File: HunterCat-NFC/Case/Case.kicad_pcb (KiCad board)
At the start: 2 copper layers, 88 x 33.5 mm, 4 parts

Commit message: Case
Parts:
- added REF**: MountingHole_2.2mm_M2, MountingHole:MountingHole_2.2mm_M2, F.Cu at (84.4, 119.8)
- added REF**: MountingHole_2.2mm_M2, MountingHole:MountingHole_2.2mm_M2, F.Cu at (189.7, 147.5)
- added REF**: MountingHole_2.2mm_M2, MountingHole:MountingHole_2.2mm_M2, F.Cu at (149.8, 35.4)
- added REF**: MountingHole_2.2mm_M2, MountingHole:MountingHole_2.2mm_M2, F.Cu at (138.4, 35.3)
- added REF**: MountingHole_2.2mm_M2, MountingHole:MountingHole_2.2mm_M2, F.Cu at (138.4, 55.6)
- added REF**: MountingHole_2.2mm_M2, MountingHole:MountingHole_2.2mm_M2, F.Cu at (149.8, 55.6)
- added REF**: MountingHole_2.2mm_M2, MountingHole:MountingHole_2.2mm_M2, F.Cu at (107.9, 31.0)
- added REF**: MountingHole_2.2mm_M2, MountingHole:MountingHole_2.2mm_M2, F.Cu at (188.5, 31.0)
- added REF**: MountingHole_2.2mm_M2, MountingHole:MountingHole_2.2mm_M2, F.Cu at (188.5, 58.7)
- added REF**: MountingHole_2.2mm_M2, MountingHole:MountingHole_2.2mm_M2, F.Cu at (83.2, 58.7)
- added REF**: MountingHole_2.2mm_M2, MountingHole:MountingHole_2.2mm_M2, F.Cu at (107.9, 58.7)
- added REF**: MountingHole_2.2mm_M2, MountingHole:MountingHole_2.2mm_M2, F.Cu at (84.4, 147.5)
- added REF**: MountingHole_2.2mm_M2, MountingHole:MountingHole_2.2mm_M2, F.Cu at (83.2, 31.0)
- added REF**: MountingHole_2.2mm_M2, MountingHole:MountingHole_2.2mm_M2, F.Cu at (83.0, 106.1)
- added REF**: MountingHole_2.2mm_M2, MountingHole:MountingHole_2.2mm_M2, F.Cu at (83.0, 78.4)
- added REF**: MountingHole_2.2mm_M2, MountingHole:MountingHole_2.2mm_M2, F.Cu at (109.1, 147.5)
- added REF**: MountingHole_2.2mm_M2, MountingHole:MountingHole_2.2mm_M2, F.Cu at (109.1, 119.8)
- added REF**: MountingHole_2.2mm_M2, MountingHole:MountingHole_2.2mm_M2, F.Cu at (139.6, 144.4)
- added REF**: MountingHole_2.2mm_M2, MountingHole:MountingHole_2.2mm_M2, F.Cu at (189.7, 119.8)
- added REF**: MountingHole_2.2mm_M2, MountingHole:MountingHole_2.2mm_M2, F.Cu at (151.1, 144.4)
- added REF**: MountingHole_2.2mm_M2, MountingHole:MountingHole_2.2mm_M2, F.Cu at (151.1, 124.2)
- added REF**: MountingHole_2.2mm_M2, MountingHole:MountingHole_2.2mm_M2, F.Cu at (139.6, 124.1)
- moved REF** 36.9 mm to (107.7, 78.4)
- moved REF** 36.9 mm to (107.7, 106.1)
- moved REF** 36.9 mm to (188.2, 106.1)
- moved REF** 36.9 mm to (188.2, 78.4)
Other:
- board size 88 x 33.5 mm -> 113.4 x 122.3 mm

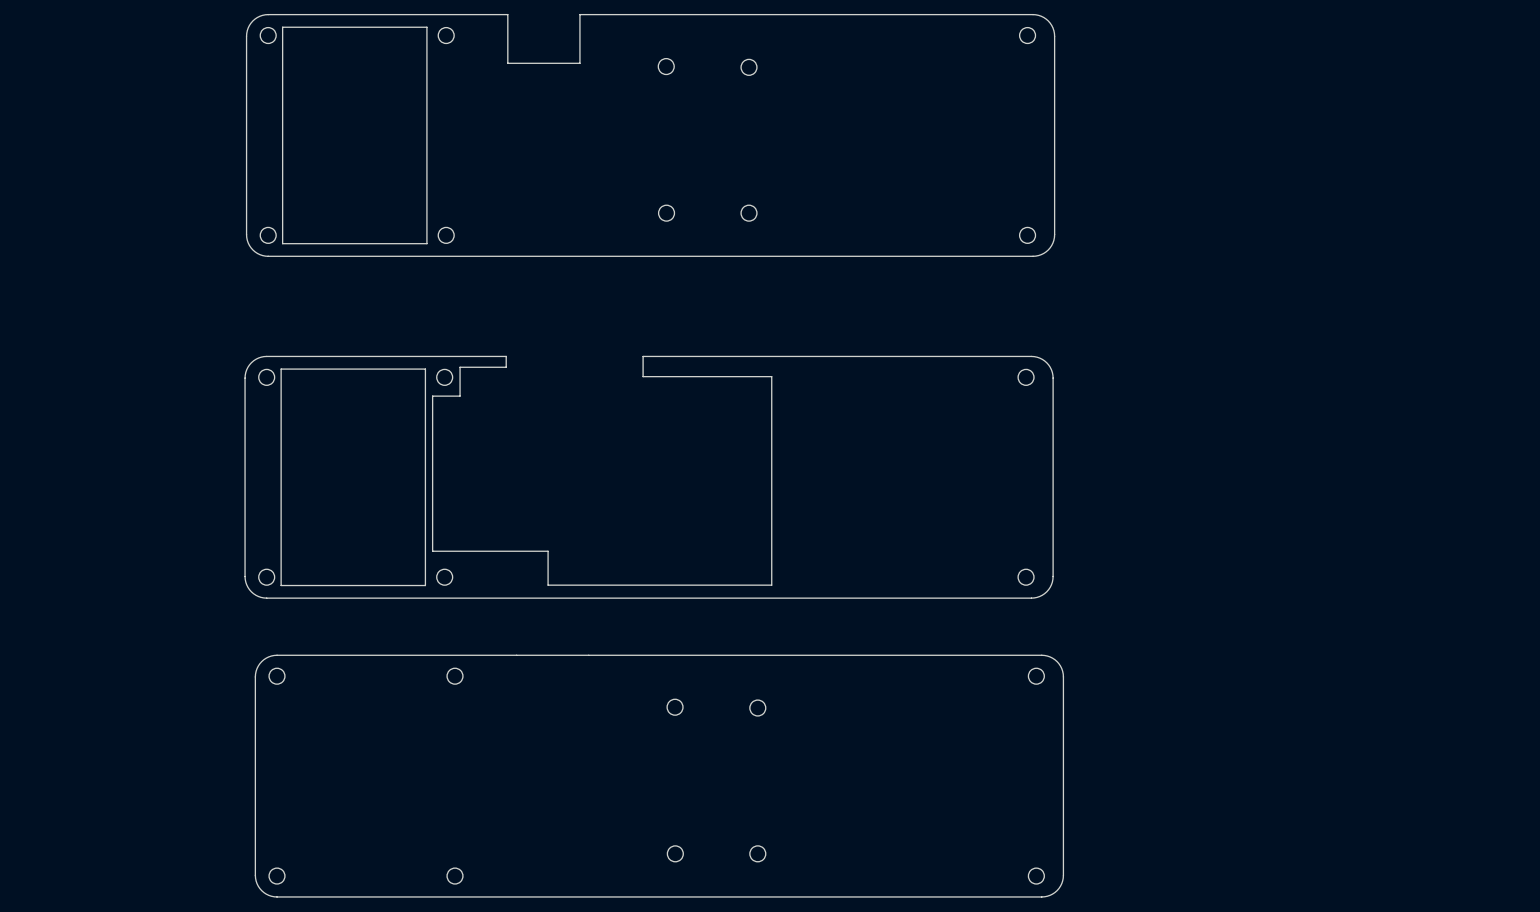
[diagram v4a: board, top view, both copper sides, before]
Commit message: Moved footprints
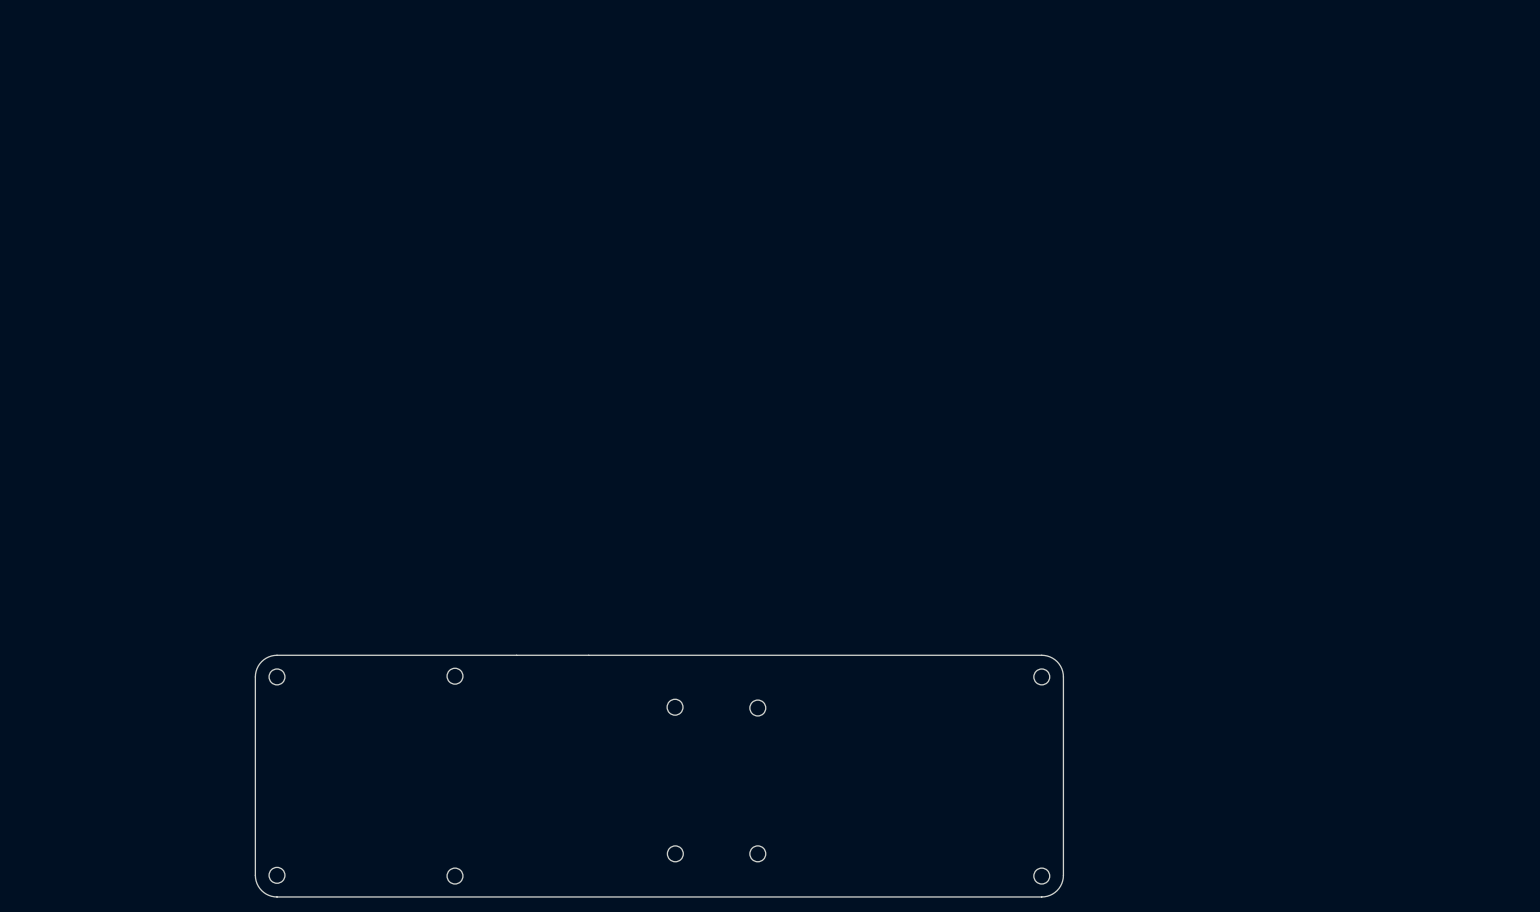
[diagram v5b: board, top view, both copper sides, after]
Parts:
- removed the REF** at (149.8, 35.4)
- removed the REF** at (138.4, 35.3)
- removed the REF** at (138.4, 55.6)
- removed the REF** at (149.8, 55.6)
- removed the REF** at (107.9, 31.0)
- removed the REF** at (188.5, 31.0)
- removed the REF** at (188.5, 58.7)
- removed the REF** at (83.2, 58.7)
- removed the REF** at (107.9, 58.7)
- removed the REF** at (83.2, 31.0)
- removed the REF** at (83.0, 106.1)
- removed the REF** at (83.0, 78.4)
- removed the REF** at (107.7, 106.1)
- removed the REF** at (188.2, 106.1)
- removed the REF** at (188.2, 78.4)
- removed the REF** at (107.7, 78.4)
- moved REF** 0.76 mm to (190.4, 119.9)
- moved REF** 0.75 mm to (190.4, 147.5)
- moved REF** 0.10 mm to (84.4, 147.4)
- moved REF** 0.10 mm to (84.4, 119.9)
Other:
- board size 113.4 x 122.3 mm -> 112 x 33.5 mm

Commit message: Case holes placement
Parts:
- removed the REF** at (109.1, 147.5)
- removed the REF** at (109.1, 119.8)
- moved REF** 31.3 mm to (170.9, 124.2)
- moved REF** 31.3 mm to (182.4, 144.4)
- moved REF** 31.3 mm to (182.4, 124.2)
- moved REF** 31.3 mm to (170.9, 144.4)
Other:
- outline, holes or cut-outs redrawn
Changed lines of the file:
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@@
   (general
     (thickness 1.6)
-    (drawings 10)
+    (drawings 18)
     (tracks 0)
     (zones 0)
-    (modules 10)
+    (modules 8)
     (nets 1)
   )
@@
   )
   (module MountingHole:MountingHole_2.2mm_M2 (layer F.Cu)
-    (at 109.1 147.52)
-    (descr "Mounting Hole 2.2mm, no annular, M2")
-    (tags "mounting hole 2.2mm no annular m2")
-    (attr virtual)
-    (fp_text reference REF** (at 0 -3.2) (layer F.Fab)
-      (effects (font (size 1 1) (thickness 0.15)))
-    )
-    (fp_text value MountingHole_2.2mm_M2 (at 0 3.2) (layer F.Fab)
-      (effects (font (size 1 1) (thickness 0.15)))
-    )
-    (fp_circle (center 0 0) (end 2.2 0) (layer Cmts.User) (width 0.15))
-    (fp_circle (center 0 0) (end 2.45 0) (layer F.CrtYd) (width 0.05))
-    (fp_text user %R (at 0.3 0) (layer F.Fab)
-      (effects (font (size 1 1) (thickness 0.15)))
-    )
-    (pad 1 np_thru_hole circle (at 0 0) (size 2.2 2.2) (drill 2.2) (layers *.Cu *.Mask))
-  )
-  (module MountingHole:MountingHole_2.2mm_M2 (layer F.Cu)
-    (at 109.1 119.82)
-    (descr "Mounting Hole 2.2mm, no annular, M2")
-    (tags "mounting hole 2.2mm no annular m2")
-    (attr virtual)
-    (fp_text reference REF** (at 0 -3.2) (layer F.Fab)
-      (effects (font (size 1 1) (thickness 0.15)))
-    )
-    (fp_text value MountingHole_2.2mm_M2 (at 0 3.2) (layer F.Fab)
-      (effects (font (size 1 1) (thickness 0.15)))
-    )
-    (fp_circle (center 0 0) (end 2.45 0) (layer F.CrtYd) (width 0.05))
-    (fp_circle (center 0 0) (end 2.2 0) (layer Cmts.User) (width 0.15))
-    (fp_text user %R (at 0.3 0) (layer F.Fab)
-      (effects (font (size 1 1) (thickness 0.15)))
-    )
-    (pad 1 np_thru_hole circle (at 0 0) (size 2.2 2.2) (drill 2.2) (layers *.Cu *.Mask))
-  )
-  (module MountingHole:MountingHole_2.2mm_M2 (layer F.Cu)
-    (at 139.64 144.44)
+    (at 170.91 144.44)
     (descr "Mounting Hole 2.2mm, no annular, M2")
     (tags "mounting hole 2.2mm no annular m2")
@@
   )
   (module MountingHole:MountingHole_2.2mm_M2 (layer F.Cu)
-    (at 151.07 144.44)
-    (descr "Mounting Hole 2.2mm, no annular, M2")
-    (tags "mounting hole 2.2mm no annular m2")
-    (attr virtual)
-    (fp_text reference REF** (at 0 -3.2) (layer F.Fab)
-      (effects (font (size 1 1) (thickness 0.15)))
-    )
-    (fp_text value MountingHole_2.2mm_M2 (at 0 3.2) (layer F.Fab)
-      (effects (font (size 1 1) (thickness 0.15)))
-    )
-    (fp_circle (center 0 0) (end 2.45 0) (layer F.CrtYd) (width 0.05))
-    (fp_circle (center 0 0) (end 2.2 0) (layer Cmts.User) (width 0.15))
-    (fp_text user %R (at 0.3 0) (layer F.Fab)
-      (effects (font (size 1 1) (thickness 0.15)))
-    )
-    (pad 1 np_thru_hole circle (at 0 0) (size 2.2 2.2) (drill 2.2) (layers *.Cu *.Mask))
-  )
-  (module MountingHole:MountingHole_2.2mm_M2 (layer F.Cu)
-    (at 151.07 124.23)
-    (descr "Mounting Hole 2.2mm, no annular, M2")
-    (tags "mounting hole 2.2mm no annular m2")
-    (attr virtual)
-    (fp_text reference REF** (at 0 -3.2) (layer F.Fab)
-      (effects (font (size 1 1) (thickness 0.15)))
-    )
-    (fp_text value MountingHole_2.2mm_M2 (at 0 3.2) (layer F.Fab)
-      (effects (font (size 1 1) (thickness 0.15)))
-    )
-    (fp_circle (center 0 0) (end 2.2 0) (layer Cmts.User) (width 0.15))
-    (fp_circle (center 0 0) (end 2.45 0) (layer F.CrtYd) (width 0.05))
-    (fp_text user %R (at 0.3 0) (layer F.Fab)
-      (effects (font (size 1 1) (thickness 0.15)))
-    )
-    (pad 1 np_thru_hole circle (at 0 0) (size 2.2 2.2) (drill 2.2) (layers *.Cu *.Mask))
-  )
-  (module MountingHole:MountingHole_2.2mm_M2 (layer F.Cu)
-    (at 139.6 124.12)
+    (at 182.38 144.44)
+    (descr "Mounting Hole 2.2mm, no annular, M2")
+    (tags "mounting hole 2.2mm no annular m2")
+    (attr virtual)
+    (fp_text reference REF** (at 0 -3.2) (layer F.Fab)
+      (effects (font (size 1 1) (thickness 0.15)))
+    )
+    (fp_text value MountingHole_2.2mm_M2 (at 0 3.2) (layer F.Fab)
+      (effects (font (size 1 1) (thickness 0.15)))
+    )
+    (fp_circle (center 0 0) (end 2.45 0) (layer F.CrtYd) (width 0.05))
+    (fp_circle (center 0 0) (end 2.2 0) (layer Cmts.User) (width 0.15))
+    (fp_text user %R (at 0.3 0) (layer F.Fab)
+      (effects (font (size 1 1) (thickness 0.15)))
+    )
+    (pad 1 np_thru_hole circle (at 0 0) (size 2.2 2.2) (drill 2.2) (layers *.Cu *.Mask))
+  )
+  (module MountingHole:MountingHole_2.2mm_M2 (layer F.Cu)
+    (at 182.38 124.23)
+    (descr "Mounting Hole 2.2mm, no annular, M2")
+    (tags "mounting hole 2.2mm no annular m2")
+    (attr virtual)
+    (fp_text reference REF** (at 0 -3.2) (layer F.Fab)
+      (effects (font (size 1 1) (thickness 0.15)))
+    )
+    (fp_text value MountingHole_2.2mm_M2 (at 0 3.2) (layer F.Fab)
+      (effects (font (size 1 1) (thickness 0.15)))
+    )
+    (fp_circle (center 0 0) (end 2.2 0) (layer Cmts.User) (width 0.15))
+    (fp_circle (center 0 0) (end 2.45 0) (layer F.CrtYd) (width 0.05))
+    (fp_text user %R (at 0.3 0) (layer F.Fab)
+      (effects (font (size 1 1) (thickness 0.15)))
+    )
+    (pad 1 np_thru_hole circle (at 0 0) (size 2.2 2.2) (drill 2.2) (layers *.Cu *.Mask))
+  )
+  (module MountingHole:MountingHole_2.2mm_M2 (layer F.Cu)
+    (at 170.91 124.23)
     (descr "Mounting Hole 2.2mm, no annular, M2")
     (tags "mounting hole 2.2mm no annular m2")
@@
     (pad 1 np_thru_hole circle (at 0 0) (size 2.2 2.2) (drill 2.2) (layers *.Cu *.Mask))
   )
+  (gr_line (start 113.06 146.08) (end 108.8 146.08) (layer Edge.Cuts) (width 0.05))
+  (gr_line (start 113.06 145.8) (end 113.06 146.08) (layer Edge.Cuts) (width 0.05))
+  (gr_line (start 108.8 145.8) (end 108.8 146.08) (layer Edge.Cuts) (width 0.05))
+  (gr_line (start 113.06 137.15) (end 108.8 137.15) (layer Edge.Cuts) (width 0.05))
+  (gr_line (start 113.06 137.43) (end 113.06 137.15) (layer Edge.Cuts) (width 0.05))
+  (gr_line (start 108.8 137.43) (end 108.8 137.15) (layer Edge.Cuts) (width 0.05))
+  (gr_line (start 113.06 137.43) (end 113.06 145.8) (layer Edge.Cuts) (width 0.05))
+  (gr_line (start 108.8 137.43) (end 108.8 145.8) (layer Edge.Cuts) (width 0.05))
   (gr_arc (start 84.43 119.92) (end 84.43 116.92) (angle -90) (layer Edge.Cuts) (width 0.05))
   (gr_arc (start 190.43 147.42) (end 190.43 150.42) (angle -90) (layer Edge.Cuts) (width 0.05))
